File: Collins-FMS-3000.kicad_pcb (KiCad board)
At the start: 2 copper layers, 145 x 160 mm, 128 parts, among them J1 USB_B_Mini, J2 AVR-ISP-6, J3 Conn_01x04, SW1 SW_Push_LED, SW10 SW_Push_LED, SW11 SW_Push_LED, SW12 SW_Push_LED, SW13 SW_Push_LED, SW14 SW_Push_LED, SW15 SW_Push_LED, SW16 SW_Push_LED, SW17 SW_Push_LED, SW18 SW_Push_LED, SW19 SW_Push_LED, SW2 SW_Push_LED, SW20 SW_Push_LED, SW21 SW_Push_LED, SW22 SW_Push_LED, SW23 SW_Push_LED, SW24 SW_Push_LED, SW25 SW_Push_LED, SW26 SW_Push_LED, SW27 SW_Push_LED, SW28 SW_Push_LED, SW29 SW_Push_LED, SW3 SW_Push_LED, SW30 SW_Push_LED, SW31 SW_Push_LED, SW32 SW_Push_LED, SW33 SW_Push_LED, SW34 SW_Push_LED, SW35 SW_Push_LED, SW36 SW_Push_LED, SW37 SW_Push_LED, SW38 SW_Push_LED, SW39 SW_Push_LED, SW4 SW_Push_LED, SW40 SW_Push_LED, SW41 SW_Push_LED, SW42 SW_Push_LED, SW43 SW_Push_LED, SW44 SW_Push_LED, SW45 SW_Push_LED, SW46 SW_Push_LED, SW47 SW_Push_LED, SW48 SW_Push_LED, SW49 SW_Push_LED, SW5 SW_Push_LED, SW50 SW_Push_LED, SW51 SW_Push_LED, SW52 SW_Push_LED, SW53 SW_Push_LED, SW54 SW_Push_LED, SW55 SW_Push_LED, SW56 SW_Push_LED, SW57 SW_Push_LED, SW58 SW_Push_LED, SW59 SW_Push_LED, SW6 SW_Push_LED, SW60 SW_Push_LED, SW61 SW_Push_LED, SW62 SW_Push_LED, SW63 SW_Push_LED, SW64 SW_Push_LED, SW65 SW_Push_LED, SW66 SW_Push_LED, SW67 SW_Push_LED, SW68 SW_Push_LED, SW69 SW_Push_LED, SW7 SW_Push_LED, SW70 SW_Push, SW8 SW_Push_LED, SW9 SW_Push_LED, U1 ATmega32U4-MU, U2 MCP23017_SO, U3 MCP23017_SO, U4 IS31FL3733B, Y1 16MHz

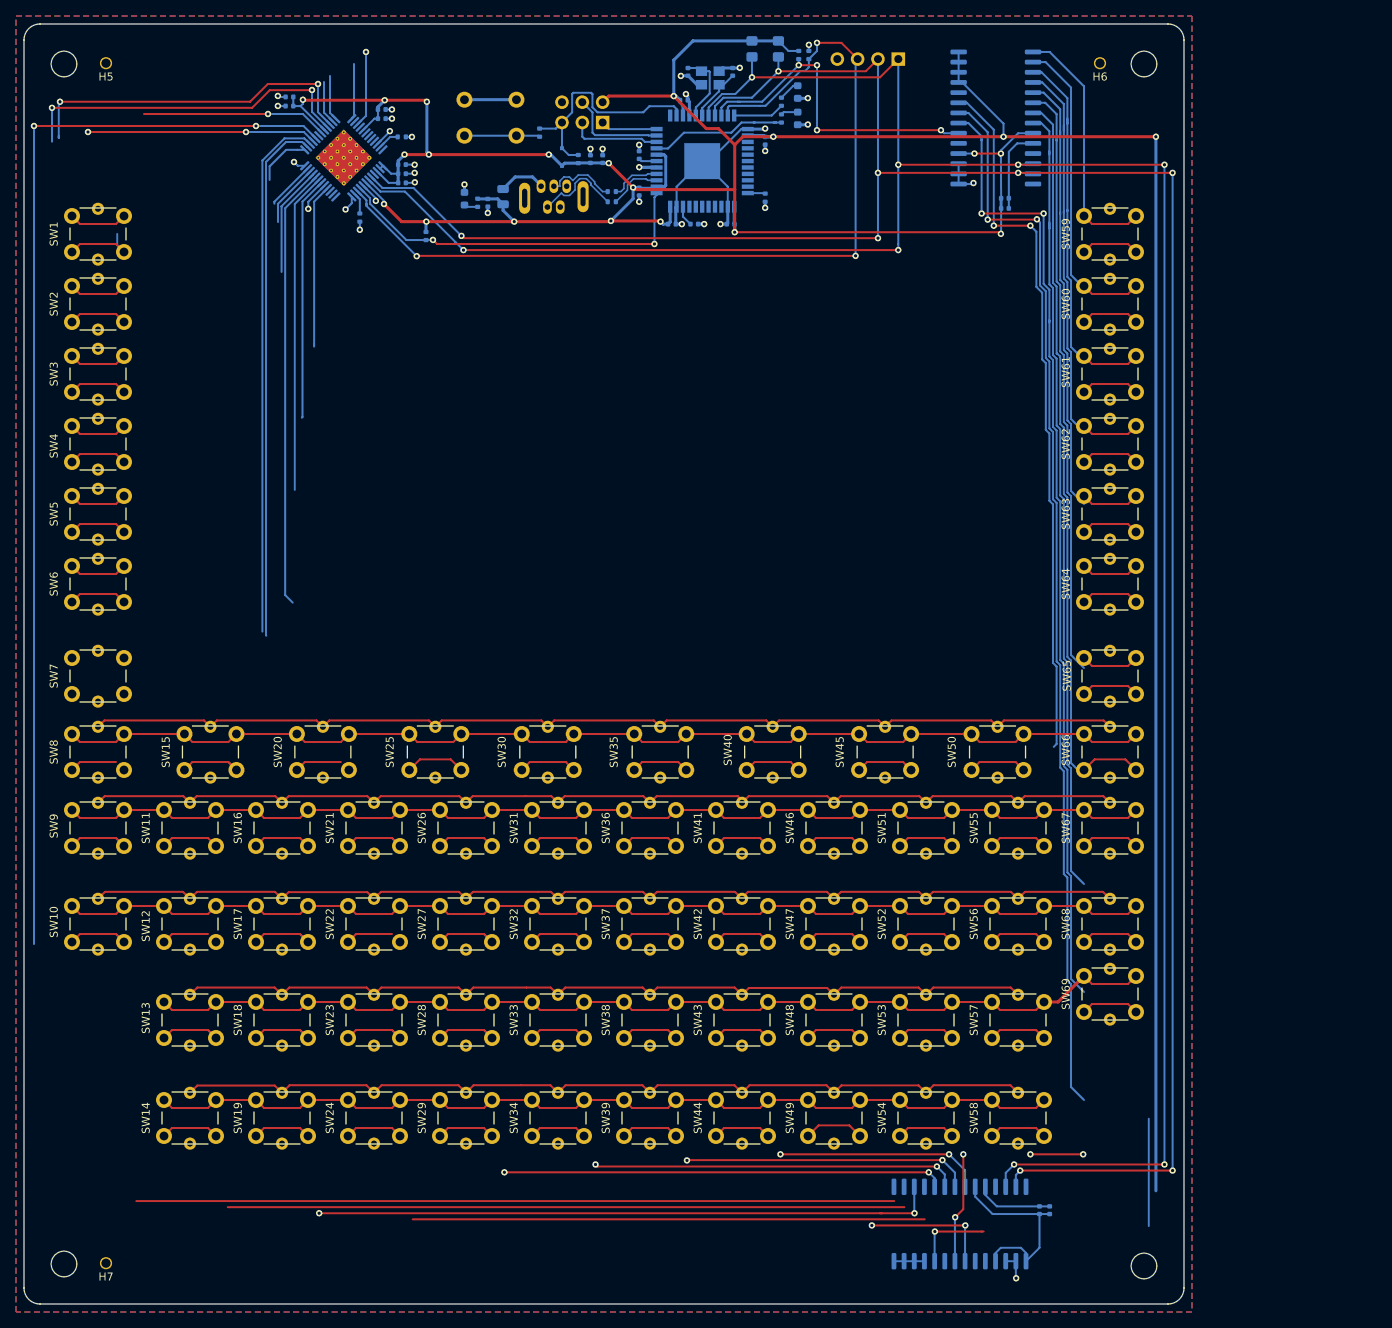
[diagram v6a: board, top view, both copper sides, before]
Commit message: Get rid of interrupt pullups, add row pullups
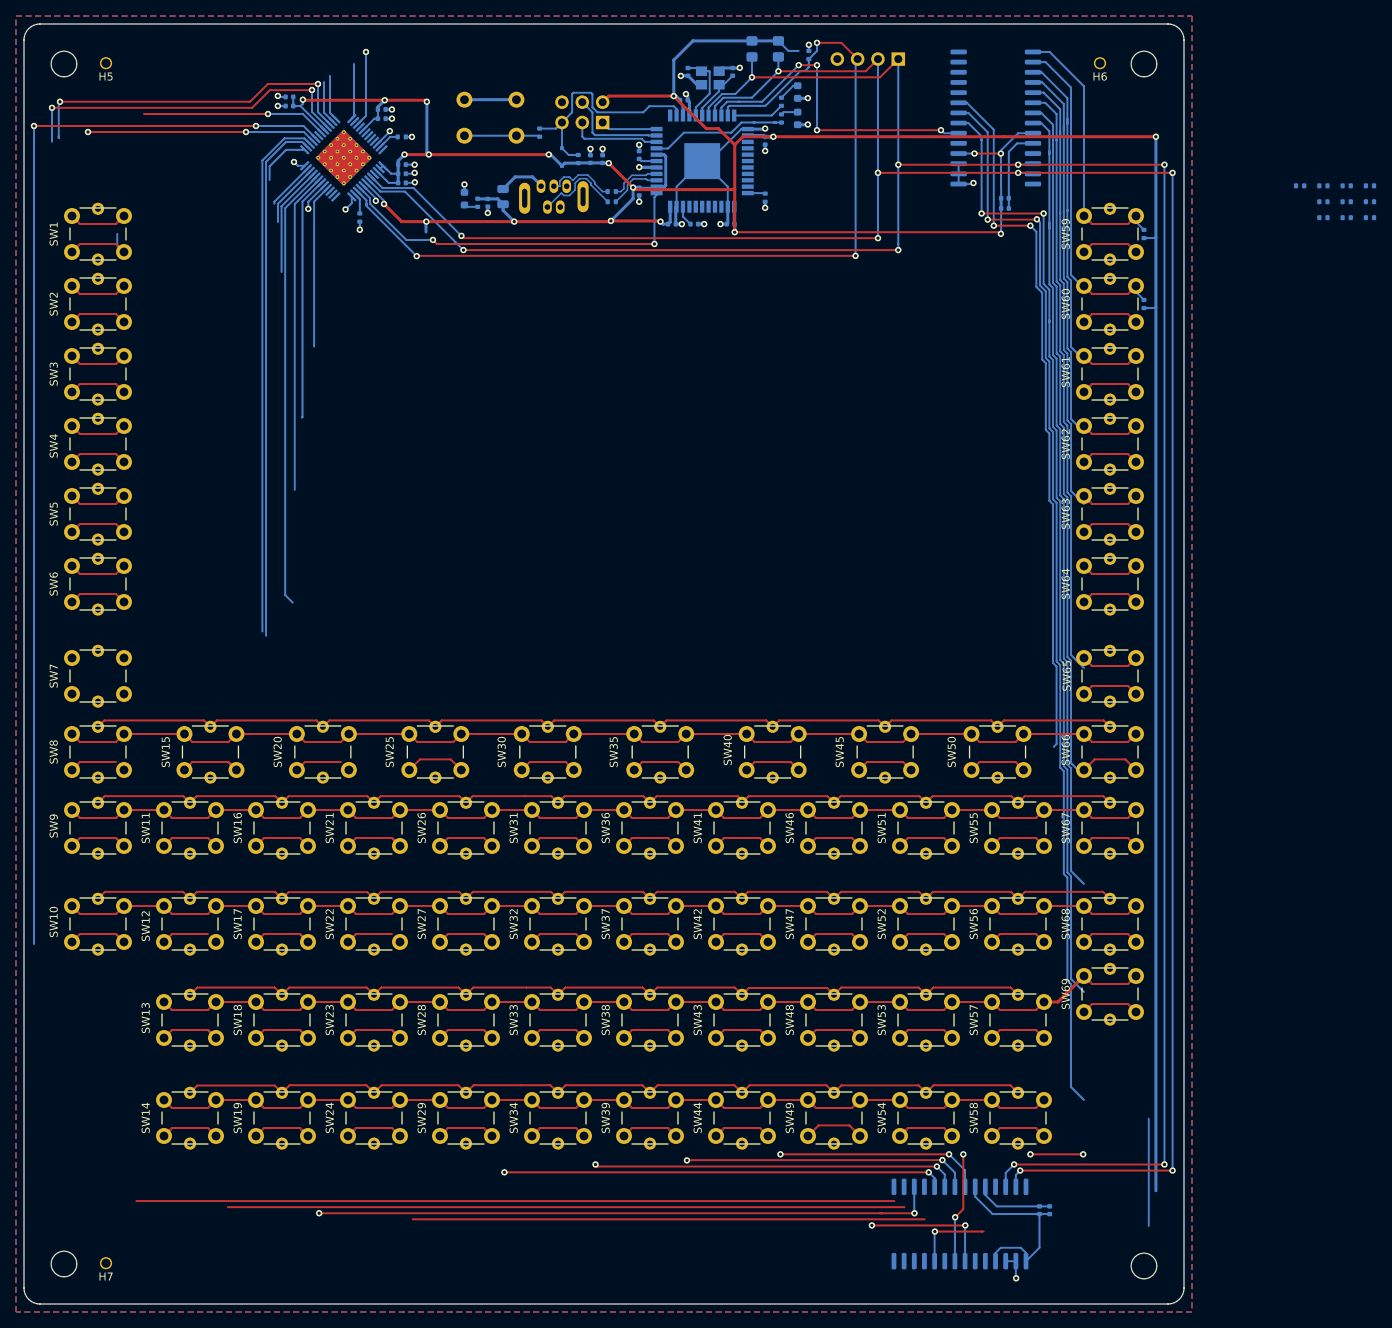
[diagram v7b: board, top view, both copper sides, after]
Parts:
- removed R4, R5: 100k, Resistor_SMD:R_0402_1005Metric
- added R10: 2k2, Resistor_SMD:R_0402_1005Metric, B.Cu at (182.4, 44.2)
- added R11: 2k2, Resistor_SMD:R_0402_1005Metric, B.Cu at (179.5, 40.2)
- added R12: 2k2, Resistor_SMD:R_0402_1005Metric, B.Cu at (182.4, 42.2)
- added R13: 2k2, Resistor_SMD:R_0402_1005Metric, B.Cu at (185.3, 44.2)
- added R14: 2k2, Resistor_SMD:R_0402_1005Metric, B.Cu at (182.4, 40.2)
- added R15: 2k2, Resistor_SMD:R_0402_1005Metric, B.Cu at (185.3, 42.2)
- added R16: 2k2, Resistor_SMD:R_0402_1005Metric, B.Cu at (188.2, 44.2)
- added R17: 2k2, Resistor_SMD:R_0402_1005Metric, B.Cu at (185.3, 40.2)
- added R18: 2k2, Resistor_SMD:R_0402_1005Metric, B.Cu at (188.2, 42.2)
- added R19: 2k2, Resistor_SMD:R_0402_1005Metric, B.Cu at (188.2, 40.2)
- added R8: 2k2, Resistor_SMD:R_0402_1005Metric, B.Cu at (160.0, 46.2)
- added R9: 2k2, Resistor_SMD:R_0402_1005Metric, B.Cu at (160.0, 55.0)
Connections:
- U2 pad 25: +5V -> Net-(U2-Pad25)
- U2 pad 26: +5V -> Net-(U2-Pad26)
- U2 pad 27: +5V -> Net-(U2-Pad27)
- U2 pad 28: +5V -> Net-(U2-Pad28)
- U3 pad 25: +5V -> Net-(U3-Pad25)
- U3 pad 26: +5V -> Net-(U3-Pad26)
- U3 pad 27: +5V -> Net-(U3-Pad27)
- U3 pad 28: +5V -> Net-(U3-Pad28)
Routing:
- net +5V: track 499.7 -> 485.8 mm, vias 21 -> 20
- net /ButtonMatrix/ROW0: track 40.4 -> 42.5 mm
- net /ButtonMatrix/ROW1: track 46.8 -> 48.9 mm
- net ROW_INTA: track 42.1 -> 41.4 mm
